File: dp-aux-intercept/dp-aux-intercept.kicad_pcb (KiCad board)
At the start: 2 copper layers, 24 parts

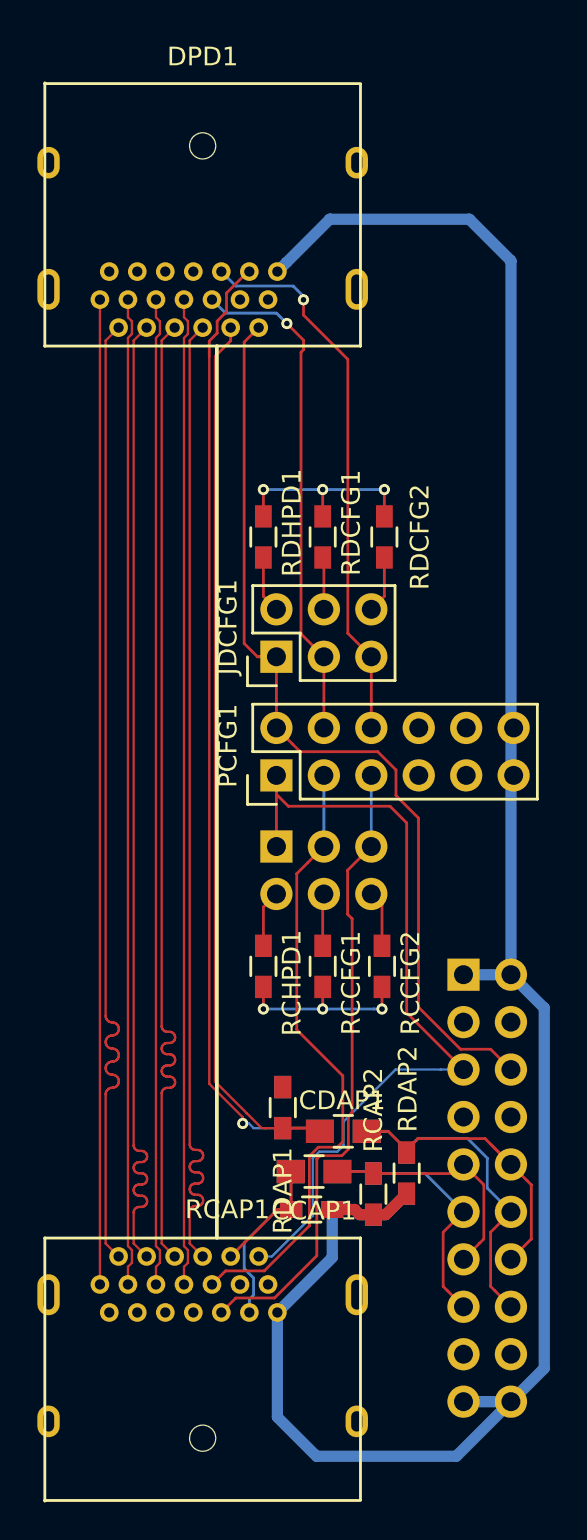
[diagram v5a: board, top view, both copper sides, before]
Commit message: Converting mm to mil.
 * 0.125mm -> 5mil (0.1270mm)
 * 0.150mm -> 6mil (0.1524mm)
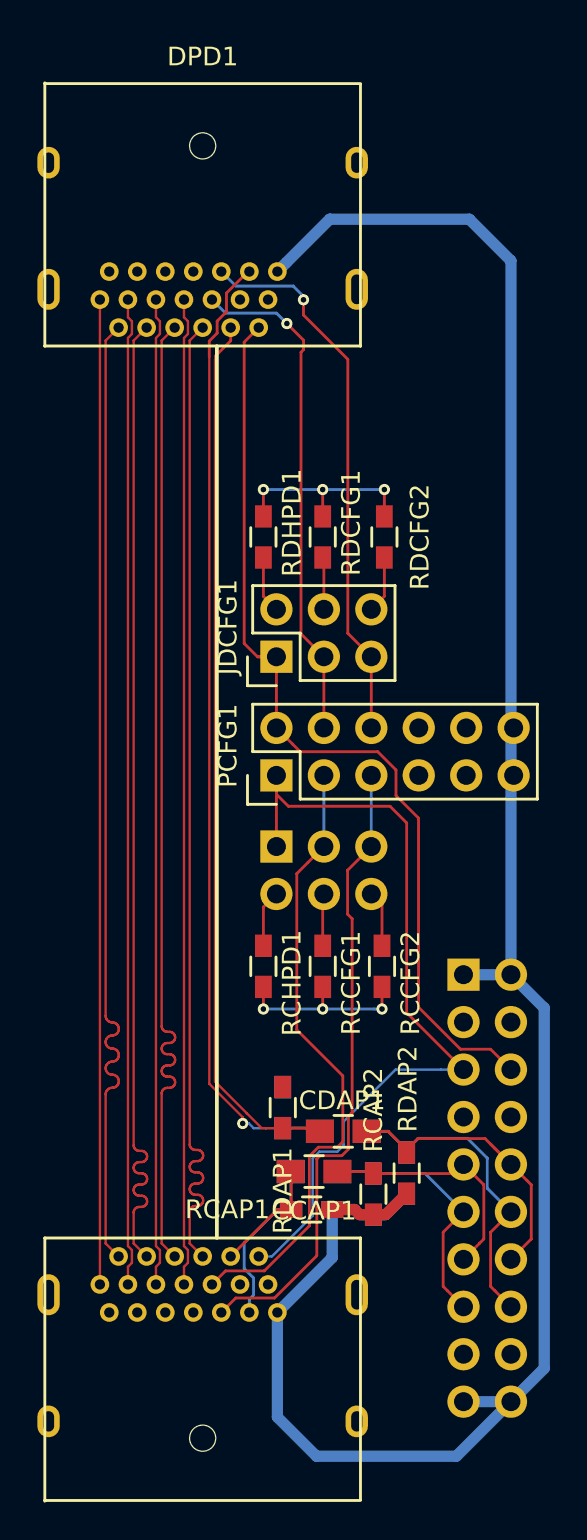
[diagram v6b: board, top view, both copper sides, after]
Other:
- net class Default: clearance 0.15 -> 0.1524; trace_width 0.125 -> 0.127
- net class VDD: clearance 0.15 -> 0.1524
- rule trace_clearance: 0.15 -> 0.1524
- rule trace_min: 0.125 -> 0.127

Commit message: Converting to 5mil/5mil + Documenting the DRC requested.
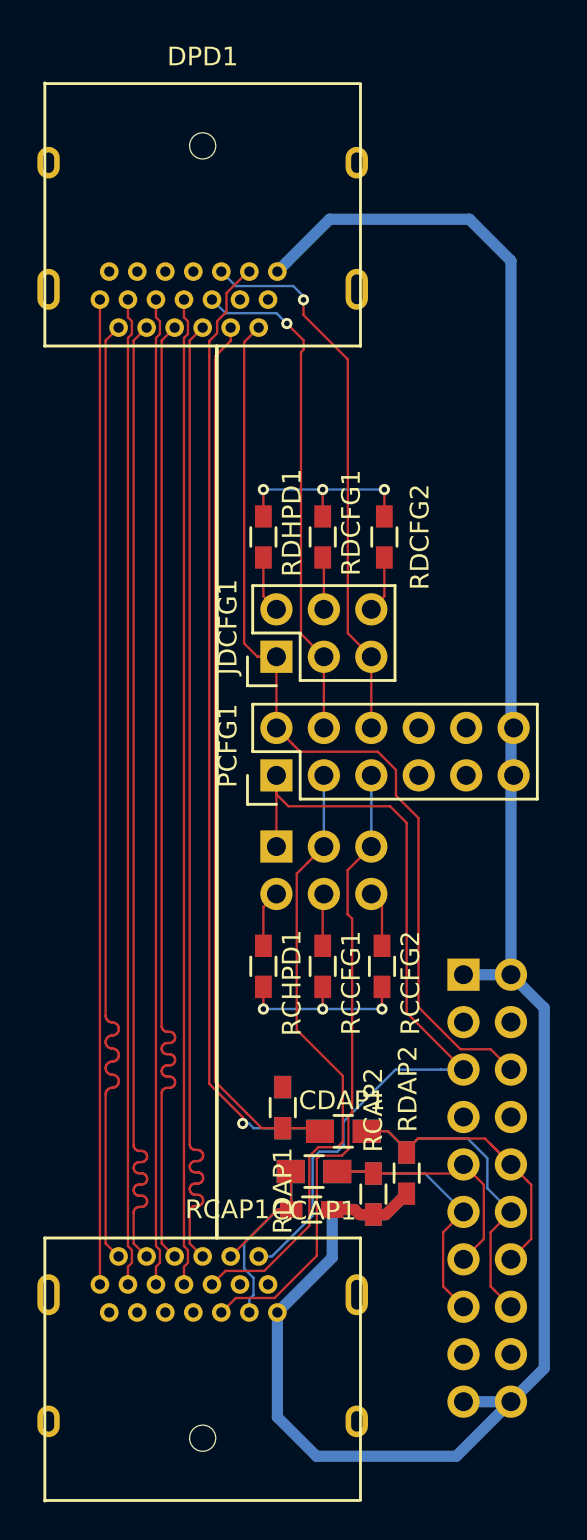
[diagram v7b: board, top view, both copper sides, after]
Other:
- net class Default: clearance 0.1524 -> 0.127
- net class VDD: clearance 0.1524 -> 0.127
- rule trace_clearance: 0.1524 -> 0.127
